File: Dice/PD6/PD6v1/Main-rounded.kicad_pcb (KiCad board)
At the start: 2 copper layers, 86.6 x 61.3 mm, 80 parts, among them J1 Conn_01x14, J2 Conn_01x11, J3 Conn_01x02, P5 COILA, P6 COILB, U1 N52810_QFN32, U2 KXTJ3-1057, U3 PJ75AL50SA, U4 LN3406, U5 MCP73832T-2ACI/OT, U6 MT9700, U7 74AHC1G08, U8 TMR1366, Y1 32MHz 40ppm

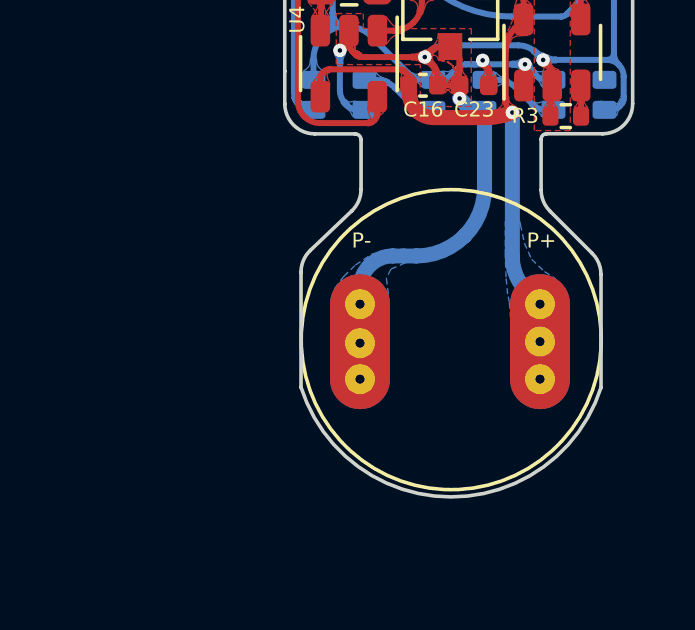
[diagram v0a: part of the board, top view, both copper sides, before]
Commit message: Update dice boards with new battery connector.
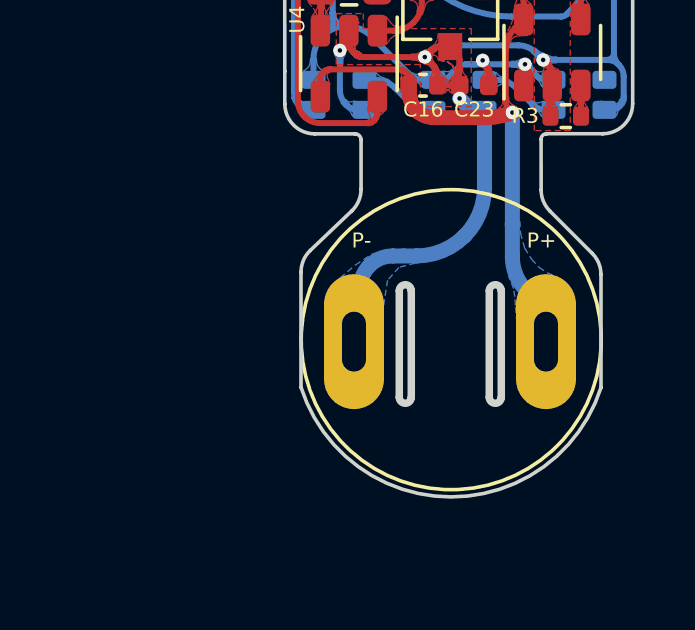
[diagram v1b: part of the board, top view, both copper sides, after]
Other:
- outline, holes or cut-outs redrawn
- board text added: "PIXELS PD6 V1 PCB SYSTEMIC GAMES"
